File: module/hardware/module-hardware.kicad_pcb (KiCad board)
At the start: 4 copper layers, 45.7 x 143.5 mm, 75 parts, among them J1 USB_B_Micro, J10 Conn_01x03, J11 Conn_01x03, J12 Conn_01x03, J2 40Pin 0.1", J3 Conn_01x02_Male, J4 40Pin 0.1", J5 Conn_01x03_Male, J6 Conn_01x03_Male, J7 Conn_01x03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

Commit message: Reorder RP2040 GPIO lines for improved routability
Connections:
- U9 pad 11: /DAC_LDACB -> /CBUS_SDIN
- U9 pad 12: /DAC_CSB -> /CBUS_DRDY
- U9 pad 13: /DAC_SCK -> /CBUS_SCK
- U9 pad 14: /DAC_SDAT -> /CBUS_SDOUT
- U9 pad 2: /CHANNEL_FULL -> unconnected-(U9-Pad2)
- U9 pad 27: /CBUS_EXTRA -> /DAC_LDACB
- U9 pad 28: /CBUS_DRDY -> /DAC_CSB
- U9 pad 29: /CBUS_SCK -> /DAC_SCK
- U9 pad 30: /CBUS_SDIN -> /DAC_SDAT
- U9 pad 31: /CBUS_SDOUT -> /CHANNEL_FULL
- U9 pad 9: unconnected-(U9-Pad9) -> /CBUS_EXTRA
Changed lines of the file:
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@@
   (net 69 "/D.R.U.M. Module Digital/FD3")
   (net 70 "unconnected-(U9-Pad8)")
-  (net 71 "unconnected-(U9-Pad9)")
-  (net 72 "/DAC_LDACB")
-  (net 73 "unconnected-(U9-Pad15)")
-  (net 74 "unconnected-(U9-Pad16)")
-  (net 75 "unconnected-(U9-Pad17)")
-  (net 76 "unconnected-(U9-Pad18)")
-  (net 77 "unconnected-(U9-Pad32)")
-  (net 78 "unconnected-(U9-Pad34)")
-  (net 79 "unconnected-(U9-Pad7)")
-  (net 80 "unconnected-(U9-Pad6)")
-  (net 81 "unconnected-(U9-Pad37)")
+  (net 71 "/DAC_LDACB")
+  (net 72 "unconnected-(U9-Pad15)")
+  (net 73 "unconnected-(U9-Pad16)")
+  (net 74 "unconnected-(U9-Pad17)")
+  (net 75 "unconnected-(U9-Pad18)")
+  (net 76 "unconnected-(U9-Pad32)")
+  (net 77 "unconnected-(U9-Pad34)")
+  (net 78 "unconnected-(U9-Pad7)")
+  (net 79 "unconnected-(U9-Pad6)")
+  (net 80 "unconnected-(U9-Pad37)")
+  (net 81 "unconnected-(U9-Pad2)")
   (footprint "Capacitor_SMD:C_0603_1608Metric_Pad1.08x0.95mm_HandSolder" (layer "F.Cu")
     (at 151.765 132.715)
@@
       (net 3 "+3V3") (pinfunction "IOVDD") (pintype "power_in"))
     (pad "2" smd roundrect locked (at -3.4375 -2.2 180) (size 0.875 0.2) (layers "F.Cu" "F.Paste" "F.Mask") (roundrect_rratio 0.25)
-      (net 48 "/CHANNEL_FULL") (pinfunction "GPIO0") (pintype "bidirectional"))
+      (net 81 "unconnected-(U9-Pad2)") (pinfunction "GPIO0") (pintype "bidirectional"))
     (pad "3" smd roundrect locked (at -3.4375 -1.8 180) (size 0.875 0.2) (layers "F.Cu" "F.Paste" "F.Mask") (roundrect_rratio 0.25)
       (net 41 "/D.R.U.M. Module Digital/GPIO1_ENC0") (pinfunction "GPIO1") (pintype "bidirectional"))
@@
       (net 39 "/D.R.U.M. Module Digital/GPIO3_ENC2") (pinfunction "GPIO3") (pintype "bidirectional"))
     (pad "6" smd roundrect locked (at -3.4375 -0.6 180) (size 0.875 0.2) (layers "F.Cu" "F.Paste" "F.Mask") (roundrect_rratio 0.25)
-      (net 80 "unconnected-(U9-Pad6)") (pinfunction "GPIO4") (pintype "bidirectional+no_connect"))
+      (net 79 "unconnected-(U9-Pad6)") (pinfunction "GPIO4") (pintype "bidirectional+no_connect"))
     (pad "7" smd roundrect locked (at -3.4375 -0.2 180) (size 0.875 0.2) (layers "F.Cu" "F.Paste" "F.Mask") (roundrect_rratio 0.25)
-      (net 79 "unconnected-(U9-Pad7)") (pinfunction "GPIO5") (pintype "bidirectional+no_connect"))
+      (net 78 "unconnected-(U9-Pad7)") (pinfunction "GPIO5") (pintype "bidirectional+no_connect"))
     (pad "8" smd roundrect locked (at -3.4375 0.2 180) (size 0.875 0.2) (layers "F.Cu" "F.Paste" "F.Mask") (roundrect_rratio 0.25)
       (net 70 "unconnected-(U9-Pad8)") (pinfunction "GPIO6") (pintype "bidirectional+no_connect"))
     (pad "9" smd roundrect locked (at -3.4375 0.6 180) (size 0.875 0.2) (layers "F.Cu" "F.Paste" "F.Mask") (roundrect_rratio 0.25)
-      (net 71 "unconnected-(U9-Pad9)") (pinfunction "GPIO7") (pintype "bidirectional+no_connect"))
+      (net 29 "/CBUS_EXTRA") (pinfunction "GPIO7") (pintype "bidirectional"))
     (pad "10" smd roundrect locked (at -3.4375 1 180) (size 0.875 0.2) (layers "F.Cu" "F.Paste" "F.Mask") (roundrect_rratio 0.25)
       (net 3 "+3V3") (pinfunction "IOVDD") (pintype "passive"))
     (pad "11" smd roundrect locked (at -3.4375 1.4 180) (size 0.875 0.2) (layers "F.Cu" "F.Paste" "F.Mask") (roundrect_rratio 0.25)
-      (net 72 "/DAC_LDACB") (pinfunction "GPIO8") (pintype "bidirectional"))
+      (net 26 "/CBUS_SDIN") (pinfunction "GPIO8") (pintype "bidirectional"))
     (pad "12" smd roundrect locked (at -3.4375 1.8 180) (size 0.875 0.2) (layers "F.Cu" "F.Paste" "F.Mask") (roundrect_rratio 0.25)
-      (net 59 "/DAC_CSB") (pinfunction "GPIO9") (pintype "bidirectional"))
+      (net 28 "/CBUS_DRDY") (pinfunction "GPIO9") (pintype "bidirectional"))
     (pad "13" smd roundrect locked (at -3.4375 2.2 180) (size 0.875 0.2) (layers "F.Cu" "F.Paste" "F.Mask") (roundrect_rratio 0.25)
-      (net 61 "/DAC_SCK") (pinfunction "GPIO10") (pintype "bidirectional"))
+      (net 27 "/CBUS_SCK") (pinfunction "GPIO10") (pintype "bidirectional"))
     (pad "14" smd roundrect locked (at -3.4375 2.6 180) (size 0.875 0.2) (layers "F.Cu" "F.Paste" "F.Mask") (roundrect_rratio 0.25)
-      (net 60 "/DAC_SDAT") (pinfunction "GPIO11") (pintype "bidirectional"))
+      (net 34 "/CBUS_SDOUT") (pinfunction "GPIO11") (pintype "bidirectional"))
     (pad "15" smd roundrect locked (at -2.6 3.4375 180) (size 0.2 0.875) (layers "F.Cu" "F.Paste" "F.Mask") (roundrect_rratio 0.25)
-      (net 73 "unconnected-(U9-Pad15)") (pinfunction "GPIO12") (pintype "bidirectional+no_connect"))
+      (net 72 "unconnected-(U9-Pad15)") (pinfunction "GPIO12") (pintype "bidirectional+no_connect"))
     (pad "16" smd roundrect locked (at -2.2 3.4375 180) (size 0.2 0.875) (layers "F.Cu" "F.Paste" "F.Mask") (roundrect_rratio 0.25)
-      (net 74 "unconnected-(U9-Pad16)") (pinfunction "GPIO13") (pintype "bidirectional+no_connect"))
+      (net 73 "unconnected-(U9-Pad16)") (pinfunction "GPIO13") (pintype "bidirectional+no_connect"))
     (pad "17" smd roundrect locked (at -1.8 3.4375 180) (size 0.2 0.875) (layers "F.Cu" "F.Paste" "F.Mask") (roundrect_rratio 0.25)
-      (net 75 "unconnected-(U9-Pad17)") (pinfunction "GPIO14") (pintype "bidirectional+no_connect"))
+      (net 74 "unconnected-(U9-Pad17)") (pinfunction "GPIO14") (pintype "bidirectional+no_connect"))
     (pad "18" smd roundrect locked (at -1.4 3.4375 180) (size 0.2 0.875) (layers "F.Cu" "F.Paste" "F.Mask") (roundrect_rratio 0.25)
-      (net 76 "unconnected-(U9-Pad18)") (pinfunction "GPIO15") (pintype "bidirectional+no_connect"))
+      (net 75 "unconnected-(U9-Pad18)") (pinfunction "GPIO15") (pintype "bidirectional+no_connect"))
     (pad "19" smd roundrect locked (at -1 3.4375 180) (size 0.2 0.875) (layers "F.Cu" "F.Paste" "F.Mask") (roundrect_rratio 0.25)
       (net 2 "GND") (pinfunction "TESTEN") (pintype "input"))
@@
       (net 46 "/RUN") (pinfunction "RUN") (pintype "input"))
     (pad "27" smd roundrect locked (at 2.2 3.4375 180) (size 0.2 0.875) (layers "F.Cu" "F.Paste" "F.Mask") (roundrect_rratio 0.25)
-      (net 29 "/CBUS_EXTRA") (pinfunction "GPIO16") (pintype "bidirectional"))
+      (net 71 "/DAC_LDACB") (pinfunction "GPIO16") (pintype "bidirectional"))
     (pad "28" smd roundrect locked (at 2.6 3.4375 180) (size 0.2 0.875) (layers "F.Cu" "F.Paste" "F.Mask") (roundrect_rratio 0.25)
-      (net 28 "/CBUS_DRDY") (pinfunction "GPIO17") (pintype "bidirectional"))
+      (net 59 "/DAC_CSB") (pinfunction "GPIO17") (pintype "bidirectional"))
     (pad "29" smd roundrect locked (at 3.4375 2.6 180) (size 0.875 0.2) (layers "F.Cu" "F.Paste" "F.Mask") (roundrect_rratio 0.25)
-      (net 27 "/CBUS_SCK") (pinfunction "GPIO18") (pintype "bidirectional"))
+      (net 61 "/DAC_SCK") (pinfunction "GPIO18") (pintype "bidirectional"))
     (pad "30" smd roundrect locked (at 3.4375 2.2 180) (size 0.875 0.2) (layers "F.Cu" "F.Paste" "F.Mask") (roundrect_rratio 0.25)
-      (net 26 "/CBUS_SDIN") (pinfunction "GPIO19") (pintype "bidirectional"))
+      (net 60 "/DAC_SDAT") (pinfunction "GPIO19") (pintype "bidirectional"))
     (pad "31" smd roundrect locked (at 3.4375 1.8 180) (size 0.875 0.2) (layers "F.Cu" "F.Paste" "F.Mask") (roundrect_rratio 0.25)
-      (net 34 "/CBUS_SDOUT") (pinfunction "GPIO20") (pintype "bidirectional"))
+      (net 48 "/CHANNEL_FULL") (pinfunction "GPIO20") (pintype "bidirectional"))
     (pad "32" smd roundrect locked (at 3.4375 1.4 180) (size 0.875 0.2) (layers "F.Cu" "F.Paste" "F.Mask") (roundrect_rratio 0.25)
-      (net 77 "unconnected-(U9-Pad32)") (pinfunction "GPIO21") (pintype "bidirectional+no_connect"))
+      (net 76 "unconnected-(U9-Pad32)") (pinfunction "GPIO21") (pintype "bidirectional+no_connect"))
     (pad "33" smd roundrect locked (at 3.4375 1 180) (size 0.875 0.2) (layers "F.Cu" "F.Paste" "F.Mask") (roundrect_rratio 0.25)
       (net 3 "+3V3") (pinfunction "IOVDD") (pintype "passive"))
     (pad "34" smd roundrect locked (at 3.4375 0.6 180) (size 0.875 0.2) (layers "F.Cu" "F.Paste" "F.Mask") (roundrect_rratio 0.25)
-      (net 78 "unconnected-(U9-Pad34)") (pinfunction "GPIO22") (pintype "bidirectional+no_connect"))
+      (net 77 "unconnected-(U9-Pad34)") (pinfunction "GPIO22") (pintype "bidirectional+no_connect"))
     (pad "35" smd roundrect locked (at 3.4375 0.2 180) (size 0.875 0.2) (layers "F.Cu" "F.Paste" "F.Mask") (roundrect_rratio 0.25)
       (net 35 "/D.R.U.M. Module Digital/GPIO4_BTN0") (pinfunction "GPIO23") (pintype "bidirectional"))
@@
       (net 36 "/D.R.U.M. Module Digital/GPIO5_BTN1") (pinfunction "GPIO24") (pintype "bidirectional"))
     (pad "37" smd roundrect locked (at 3.4375 -0.6 180) (size 0.875 0.2) (layers "F.Cu" "F.Paste" "F.Mask") (roundrect_rratio 0.25)
-      (net 81 "unconnected-(U9-Pad37)") (pinfunction "GPIO25") (pintype "bidirectional+no_connect"))
+      (net 80 "unconnected-(U9-Pad37)") (pinfunction "GPIO25") (pintype "bidirectional+no_connect"))
     (pad "38" smd roundrect locked (at 3.4375 -1 180) (size 0.875 0.2) (layers "F.Cu" "F.Paste" "F.Mask") (roundrect_rratio 0.25)
       (net 37 "/D.R.U.M. Module Digital/GPIO26_ADC0") (pinfunction "GPIO26_ADC0") (pintype "bidirectional"))

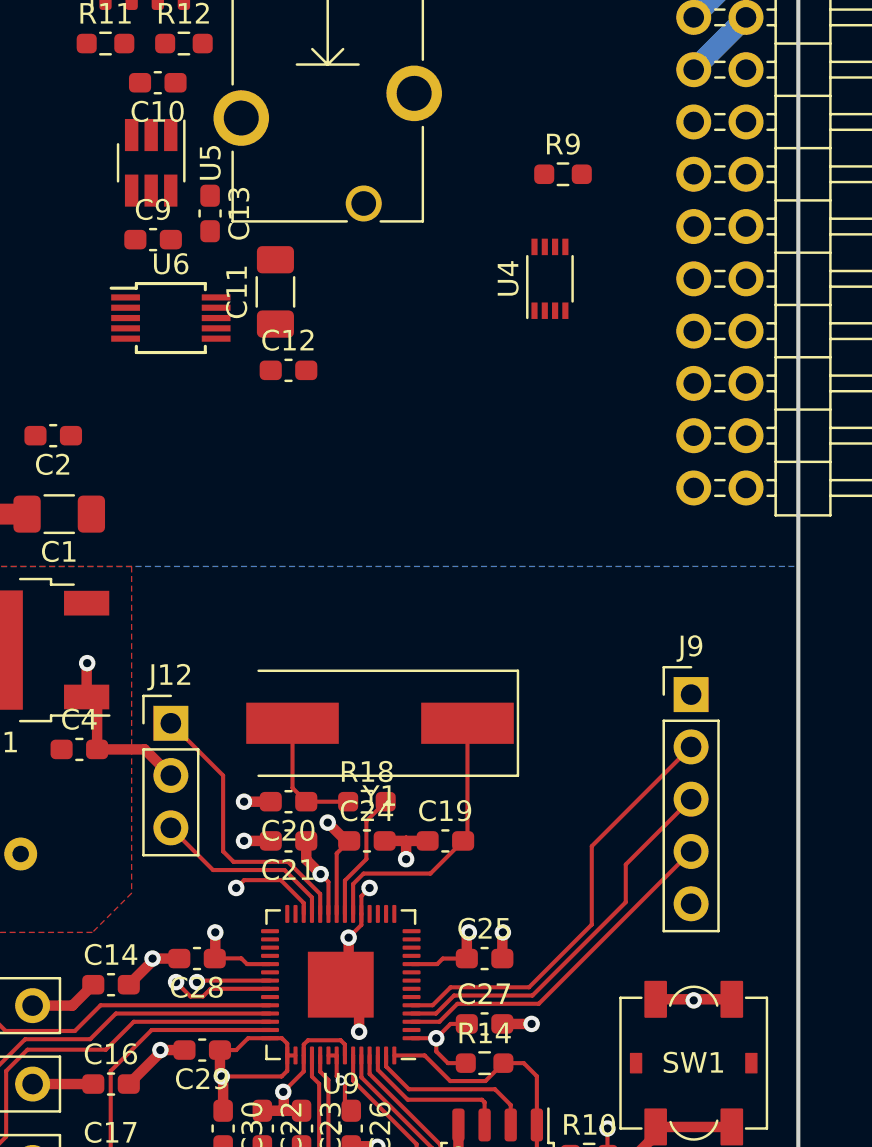
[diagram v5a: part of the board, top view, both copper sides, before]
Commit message: Route global SPI bus
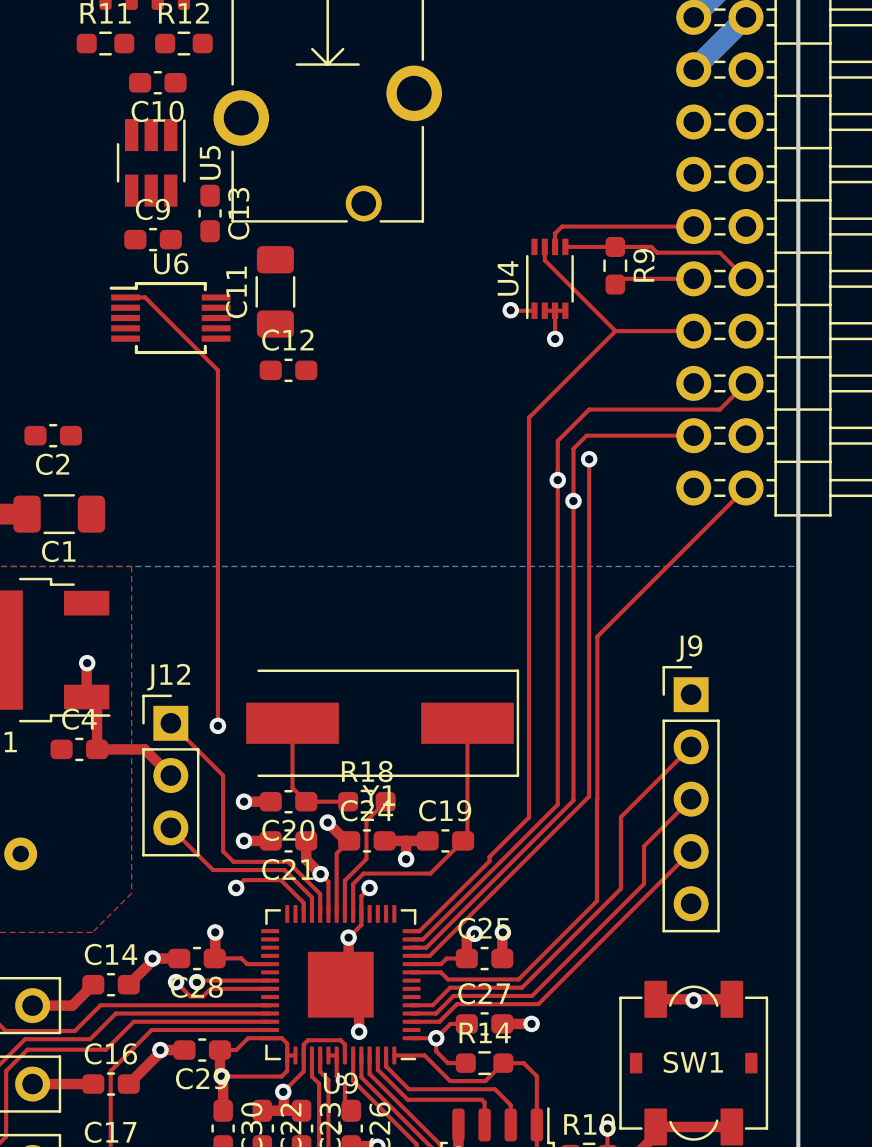
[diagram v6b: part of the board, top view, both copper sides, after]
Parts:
- moved R9 5.12 mm to (160.0, 104.8), turned to -90 degrees
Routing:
- net /CBUS_EXTRA: track 0.00 -> 75.8 mm
- net /CBUS_SCK: track 0.00 -> 71.7 mm, vias 0 -> 1
- net /CBUS_DRDY: track 0.00 -> 65.4 mm, vias 0 -> 1
- net /CBUS_SDIN: track 0.00 -> 61.3 mm, vias 0 -> 1
- net /CBUS_SDOUT: track 0.00 -> 42.8 mm
- net /RUN: track 41.8 -> 73.3 mm, vias 2 -> 3
- net /CBUS_SDRETOUT: track 0.00 -> 29.5 mm, vias 0 -> 1
- net /CBUS_NEXTPRSNT: track 0.00 -> 9.42 mm
- net /CBUS_SDRETIN: track 0.00 -> 7.53 mm
- net GND: track 75.4 -> 81.7 mm, vias 22 -> 23

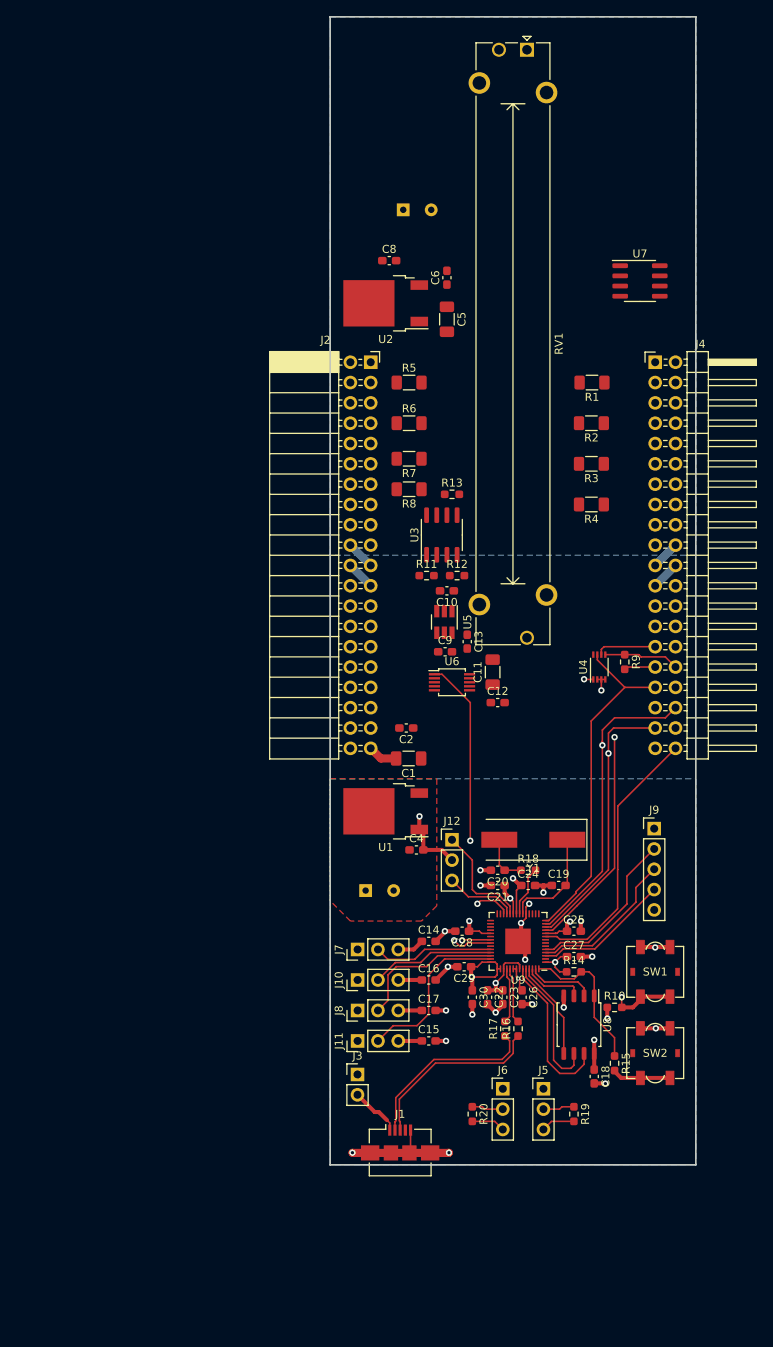
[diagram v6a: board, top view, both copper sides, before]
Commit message: Replace slidepot with slidepot daughterboard
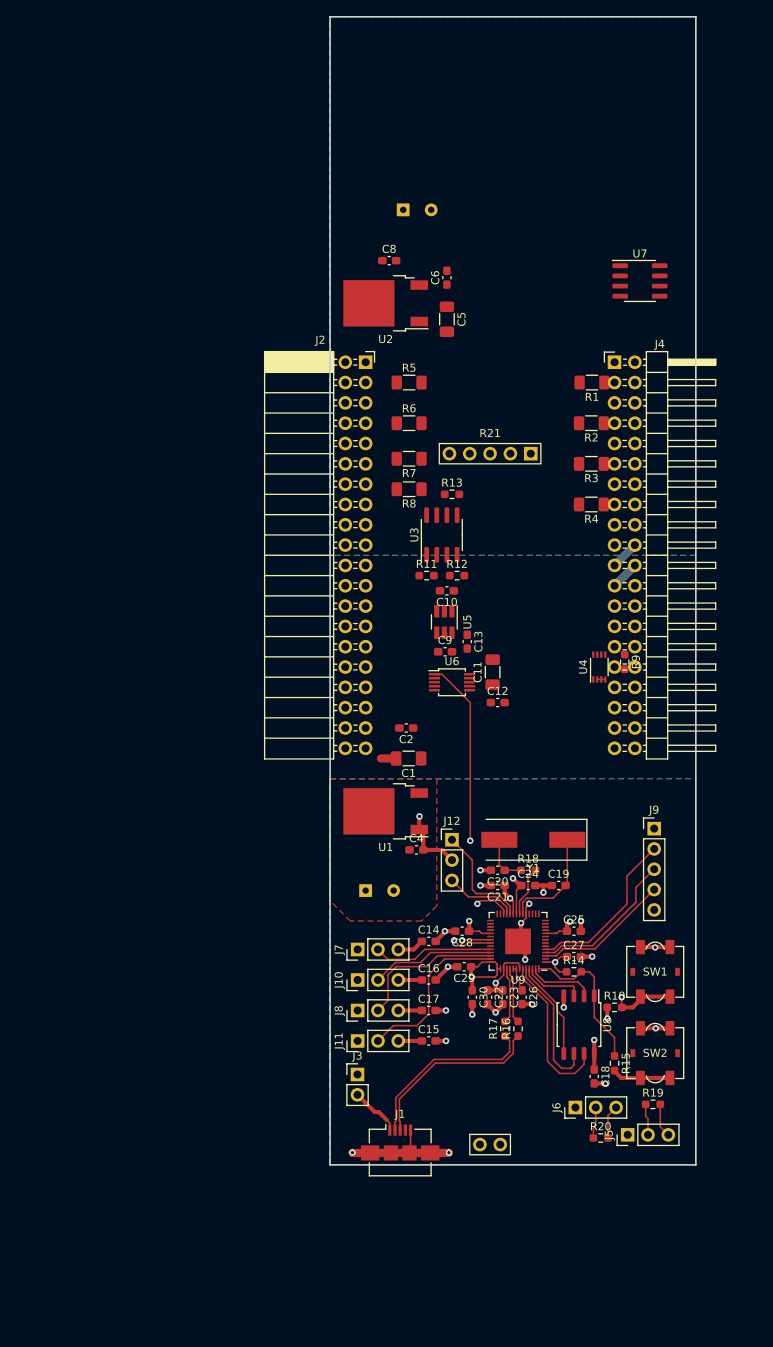
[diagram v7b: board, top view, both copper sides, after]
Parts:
- removed RV1: 10k Linear Pot, Potentiometer_THT:Potentiometer_Bourns_PTA6043_Single_Slide
- added R21: LINPOT-10KDB, custom:LINPOT-10KDB, F.Cu at (143.2, 121.9)
- moved R20 16.3 mm to (157.0, 164.3), turned to 0 degrees
- moved J5 12.0 mm to (160.4, 163.9), turned to 90 degrees
- moved R19 9.96 mm to (163.6, 160.1), turned to 0 degrees
- moved J6 9.37 mm to (153.9, 160.5), turned to 90 degrees
- moved J4 5.08 mm to (158.8, 67.3)
- moved J2 0.64 mm to (127.6, 67.3)
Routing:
- net /CBUS_EXTRA: track 75.8 -> 0.00 mm
- net /CBUS_SCK: track 71.7 -> 0.00 mm, vias 1 -> 0
- net /CBUS_DRDY: track 65.4 -> 0.00 mm, vias 1 -> 0
- net /CBUS_SDIN: track 61.3 -> 0.00 mm, vias 1 -> 0
- net /CBUS_SDOUT: track 42.8 -> 0.00 mm
- net /CBUS_SDRETOUT: track 29.5 -> 0.00 mm, vias 1 -> 0
- net /D.R.U.M. Module Digital/GPIO4_BTN0: track 32.8 -> 48.1 mm
- net GND: track 81.7 -> 71.1 mm, vias 23 -> 22
- net /CBUS_NEXTPRSNT: track 9.42 -> 0.00 mm
- net /D.R.U.M. Module Digital/GPIO5_BTN1: track 32.6 -> 41.7 mm
- net /CBUS_SDRETIN: track 7.53 -> 0.00 mm
- net GNDA: track 7.18 -> 3.59 mm

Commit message: Correct direction of input/output connectors for digital signals
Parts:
- moved U7 25.9 mm to (141.0, 72.4), turned to 90 degrees
- moved U4 5.85 mm to (151.1, 104.1)
- moved R9 5.08 mm to (154.9, 104.8)
- moved R1 2.26 mm to (153.7, 69.8)
- moved R2 1.91 mm to (153.9, 74.9)
- moved R3 1.91 mm to (153.9, 80.0)
- moved R4 1.91 mm to (153.9, 85.1)
- turned R5 to 180 degrees
- turned R6 to 180 degrees
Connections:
- J2 pad 29: /CBUS_SDRETOUT -> /CBUS_SDRETIN
- J2 pad 32: +5VD -> /CBUS_NEXTPRSNT
- J2 pad 33: /CBUS_SDIN -> /CBUS_SDOUT
- J2 pad 39: GND -> +5VD
- J4 pad 29: /CBUS_SDRETIN -> /CBUS_SDRETOUT
- J4 pad 32: /CBUS_NEXTPRSNT -> +5VD
- J4 pad 33: /CBUS_SDOUT -> /CBUS_SDIN
- J4 pad 39: GND -> +5VD
- R21 pad 3: Net-(R21-Pad3) -> GNDA
- R21 pad 4: GNDA -> Net-(R21-Pad4)
- U7 pad 3: Net-(R21-Pad3) -> Net-(R21-Pad4)
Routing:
- net /Audio Out: track 0.00 -> 5.48 mm
- net /A8: track 0.00 -> 4.67 mm
- net Net-(R21-Pad4): track 0.00 -> 4.27 mm
- net /A6: track 0.00 -> 4.15 mm
- net GNDA: track 3.59 -> 7.60 mm
- net /A4: track 0.00 -> 3.89 mm
- net /A2: track 0.00 -> 3.89 mm
- net /A1: track 0.00 -> 3.53 mm
- net /A7: track 0.00 -> 3.25 mm
- net /A5: track 0.00 -> 3.25 mm
- net /A3: track 0.00 -> 3.25 mm
- net GND: track 71.1 -> 68.2 mm
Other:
- board size 45.7 x 143.5 mm -> 45.7 x 102.9 mm
